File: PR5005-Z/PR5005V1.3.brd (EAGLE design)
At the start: 100 x 80 mm, 28 parts, among them U1 TPA2005D1DGN

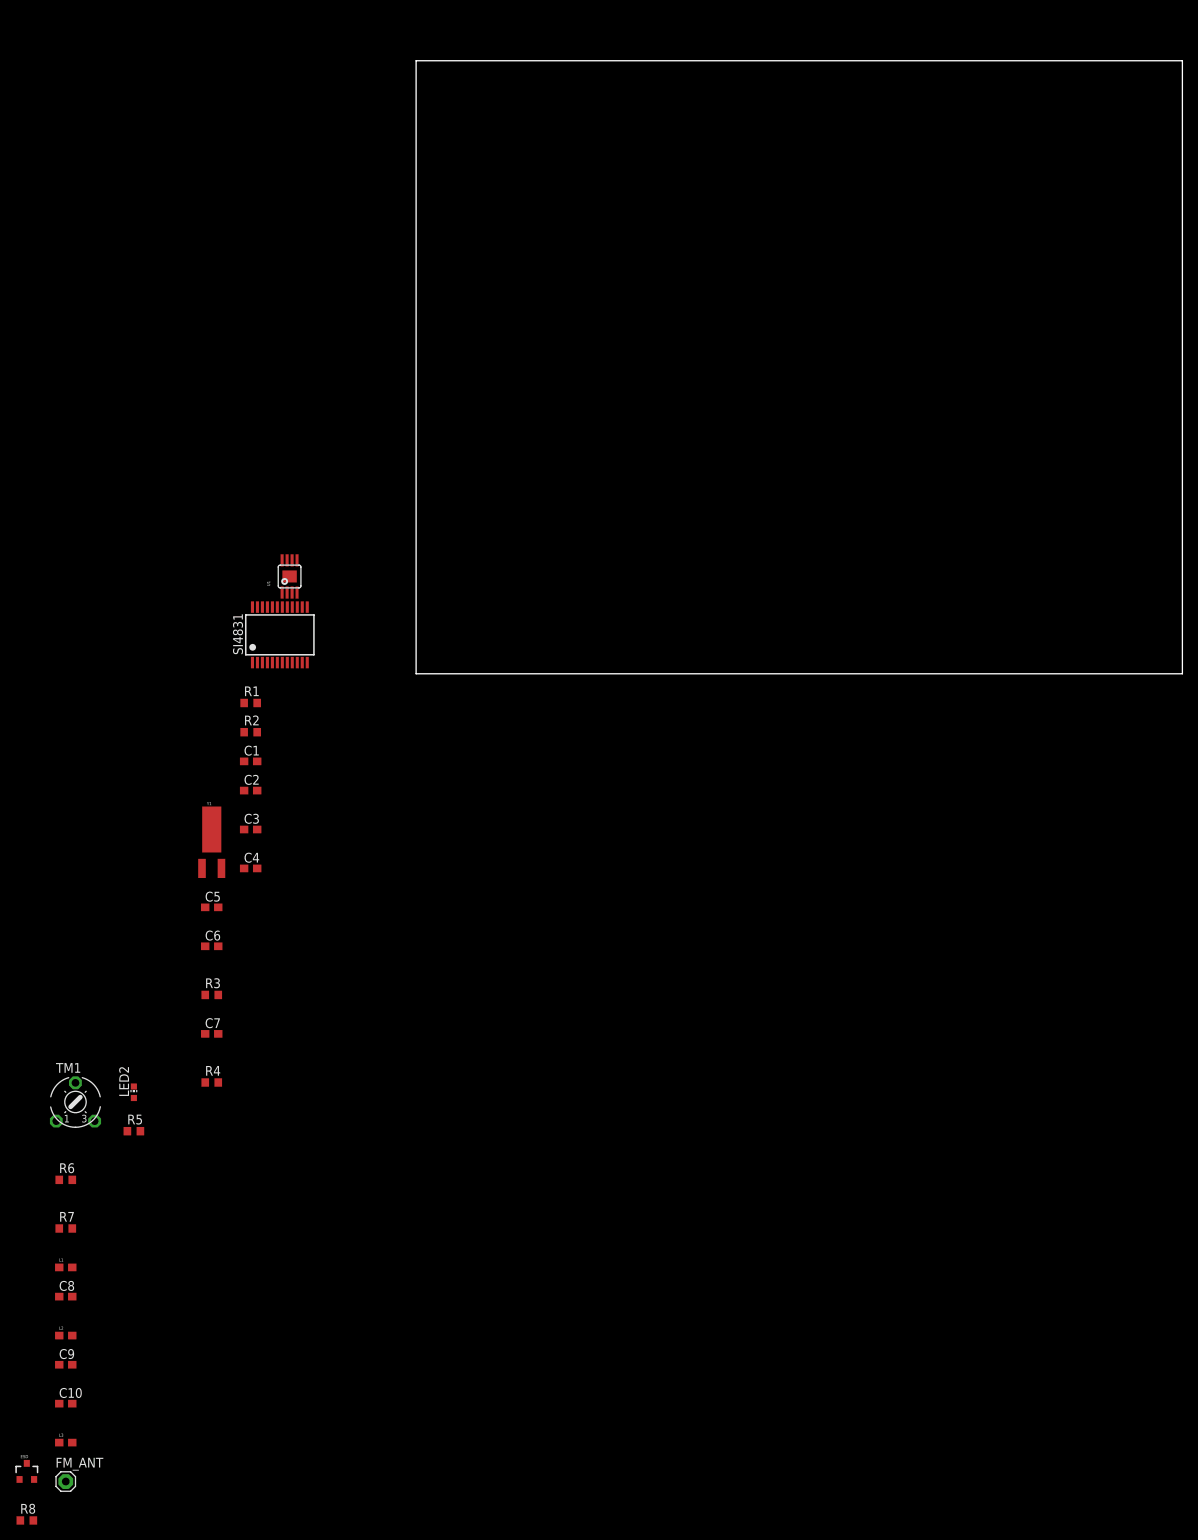
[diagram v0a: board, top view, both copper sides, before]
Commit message: PR5005 V1.3
Updated schematic.  Began board layout.
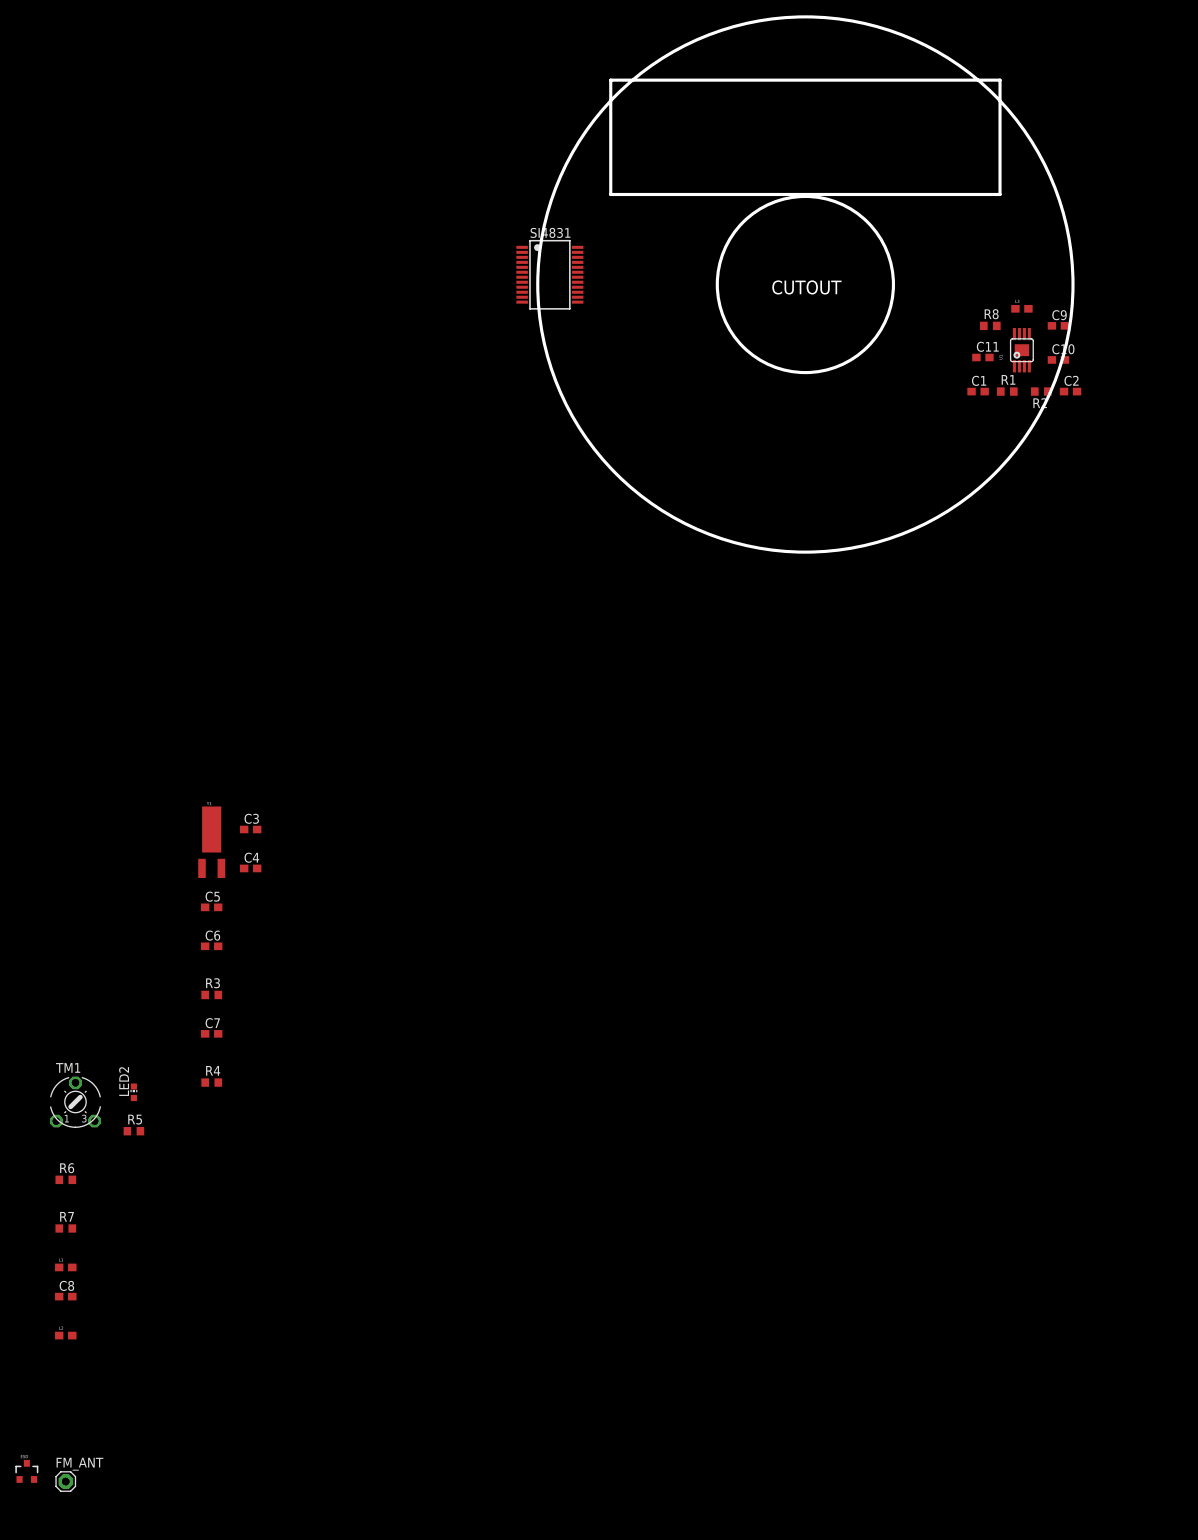
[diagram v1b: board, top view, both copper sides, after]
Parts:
- added C11: 10uf, resistor:C0603
- moved R8 200.3 mm to (74.9, 45.4)
- moved L3 193.5 mm to (79.1, 47.6)
- moved C10 188.0 mm to (83.8, 41.0)
- moved C9 187.5 mm to (83.8, 45.4)
- moved C2 119.0 mm to (85.4, 36.8)
- moved R2 112.4 mm to (81.6, 36.8), turned to 180 degrees
- moved R1 106.8 mm to (77.2, 36.8)
- moved C1 106.5 mm to (73.3, 36.8)
- moved U1 100.0 mm to (79.1, 42.2)
- moved SI4831 58.7 mm to (17.5, 52.1), turned to 270 degrees
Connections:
- net GND: now also C11.2
- net N$18: now also C11.1
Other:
- board size 100 x 80 mm -> 69.8 x 69.8 mm
- board text added: "CUTOUT"

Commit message: PR V1.3
Updated Schematic and Layout
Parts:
- removed LED2: (no value), adafruit:CHIP-LED0603
- removed SI4831: (no value), PublicRadioICs:SI4831-SSOP-24
- removed TM1: 100K, adafruit:6MM
- removed U1: TPA2005D1DGN, SparkFun-AnalogIC:POWER-SOP8
- added AMP: TPA2005D1DGN, SparkFun-AnalogIC:POWER-SOP8
- added C12: 10uf, resistor:C0603
- added C13: 1uf, resistor:C0603
- added LED1: (no value), adafruit:CHIP-LED0603
- added R9: 59K, resistor:R0603
- added SI1: (no value), PublicRadioICs:SI4831-SSOP-24
- added SPK+, SPK-: (no value), adafruit:1X01
- added TUNE: 100K, adafruit:6MM
- added U$1, U$2: MPD-BK-92-AA-CLIP, BatteryPack:MPD-BK-92-AA-CLIP
- C1: value 1uf -> 47uF
- C11: value 10uf -> 1uf
- C2: value 1uf -> .1uF
- C3: value .1uf -> 1nF
- C4: value 4.7uf -> .1uf
- C5: value 22pF -> .1uf
- C7: value .1uf -> 4.7uf
- C8: value 1nF -> 22pF
- FM_ANT: value (none) -> MOUNT-PAD-ROUND3.2; device adafruit:1X01 -> holes:3,2-PAD
- R1: value 59K -> 412K
- R2: value 59K -> 77K
- R3: value 100K -> 1K
- R6: value 77K -> 100K
- R7: value 413K -> 59K
- moved L2 168.8 mm to (35.6, 61.6)
- moved C8 166.9 mm to (47.9, 56.8), turned to 90 degrees
- moved ESD 159.8 mm to (23.2, 37.5), turned to 90 degrees
- moved FM_ANT 152.3 mm to (18.7, 32.5)
- moved R6 147.3 mm to (42.2, 52.1), turned to 90 degrees
- moved R5 140.0 mm to (31.4, 62.5), turned to 180 degrees
- moved L1 137.3 mm to (23.8, 41.0)
- moved R4 127.0 mm to (27.9, 61.3), turned to 90 degrees
- moved C7 124.6 mm to (42.2, 56.8), turned to 90 degrees
- moved C6 115.8 mm to (47.9, 53.0), turned to 270 degrees
- moved R3 113.5 mm to (27.9, 57.6), turned to 90 degrees
- moved C5 113.0 mm to (45.1, 56.8), turned to 90 degrees
- moved Y1 111.8 mm to (51.4, 54.6), turned to 270 degrees
- moved R7 110.3 mm to (35.2, 2.54)
- moved C4 97.7 mm to (42.2, 48.6), turned to 90 degrees
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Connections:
- new net N$20: R1.2, R3.1
- new net N$21: C1.1, C2.1, R3.2, SI1.3, TUNE.A
- new net N$23: AMP.5, SPK+.1
- new net N$24: AMP.8, SPK-.1
- net GND: now also AMP.7, AMP.9, C1.2, C12.2, C13.2, C4.1, C8.2, R2.1, SI1.10, SI1.11, SI1.13, SI1.14, SI1.16, SI1.17, SI1.9, TUNE.E, U$2.-, U$2.-1; no longer C5.2, C7.1, C9.2, R6.1, SI4831.10, SI4831.11, SI4831.13, SI4831.14, SI4831.16, SI4831.17, SI4831.9, TM1.E, U1.7, U1.9
- net N$1: now also AMP.3, R7.2; no longer R1.2, U1.3
- net N$10: now also SI1.18, Y1.X2; no longer SI4831.18, Y1.X1
- net N$11: now also LED1.A; no longer LED2.A
- net N$12: now also SI1.4, TUNE.S; no longer SI4831.4, TM1.S
- net N$13: now also R1.1, R2.2, SI1.5; no longer R6.2, R7.2, SI4831.5
- net N$14: now also U$1.-, U$1.-1, U$2.+, U$2.+1; no longer R7.1, SI4831.3, TM1.A
- net N$15: now also C3.2, SI1.8; no longer C8.2, SI4831.8
- net N$16: now also C5.1, C7.1, SI1.20, SI1.21; no longer C3.1, C4.1, SI4831.20, SI4831.21
- net N$17: now also AMP.6, C12.1, C13.1; no longer C10.1, C9.1, U1.6
- net N$18: now also AMP.1, C10.1; no longer C11.1, U1.1
- net N$19: now also C3.1, FM_ANT.B3,2; no longer C8.1, FM_ANT.1
- net N$2: now also AMP.4, R9.2; no longer R2.2, U1.4
- net N$3: now also C11.1, R9.1; no longer C2.1, R2.1
- net N$4: now also C9.2, R7.1; no longer C1.2, R1.1
- net N$5: now also C9.1, SI1.24; no longer C1.1, SI4831.24
- net N$6: now also C5.2, C7.2, SI1.22; no longer C3.2, C4.2, SI4831.22
- net N$7: now also C8.1, SI1.19, Y1.X1; no longer C5.1, SI4831.19, Y1.X2
- net N$8: now also C4.2, R6.1, SI1.15; no longer C7.2, R3.1, SI4831.15
- net N$9: now also LED1.C, SI1.2; no longer LED2.C, SI4831.2
- net VCC: now also R6.2, U$1.+, U$1.+1; no longer R3.2
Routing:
- net N$14: track 0.00 -> 62.4 mm
- net N$12: track 0.00 -> 39.1 mm, vias 0 -> 2
- net N$21: track 0.00 -> 38.1 mm
- net VCC: track 0.00 -> 20.7 mm
- net N$23: track 0.00 -> 20.0 mm, vias 0 -> 1
- net N$15: track 0.00 -> 19.9 mm
- net N$24: track 0.00 -> 17.2 mm, vias 0 -> 1
- net N$7: track 0.00 -> 12.7 mm
- net N$10: track 0.00 -> 12.3 mm
- net N$13: track 0.00 -> 11.6 mm
- net N$18: track 0.00 -> 10.1 mm
- net N$19: track 0.00 -> 9.20 mm
- net N$20: track 0.00 -> 8.00 mm
- net N$17: track 0.00 -> 7.53 mm
- net N$9: track 0.00 -> 6.99 mm
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- added copper zone on layer 1, net GND
- added copper zone on layer 16, net N$22
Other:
- board size 69.8 x 69.8 mm -> 70 x 70 mm
